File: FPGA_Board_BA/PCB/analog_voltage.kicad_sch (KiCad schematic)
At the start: 10 parts, among them U8 TPS61022

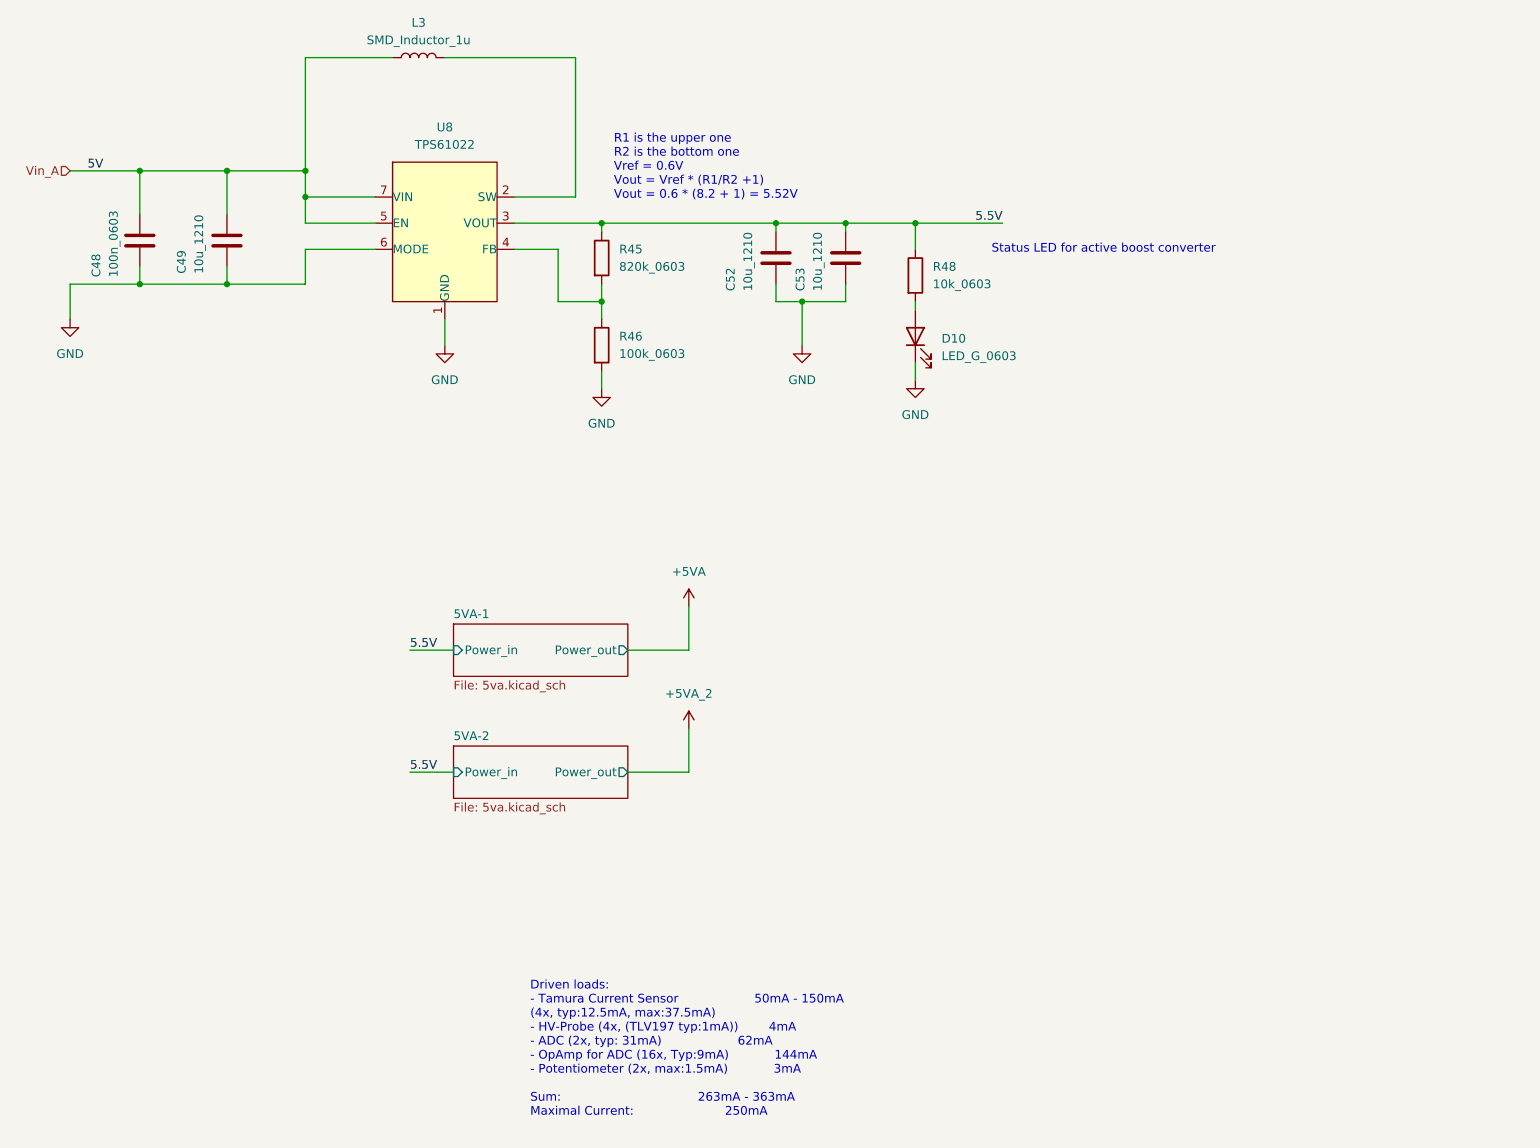
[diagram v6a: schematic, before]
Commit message: added 5V supply for Zynq
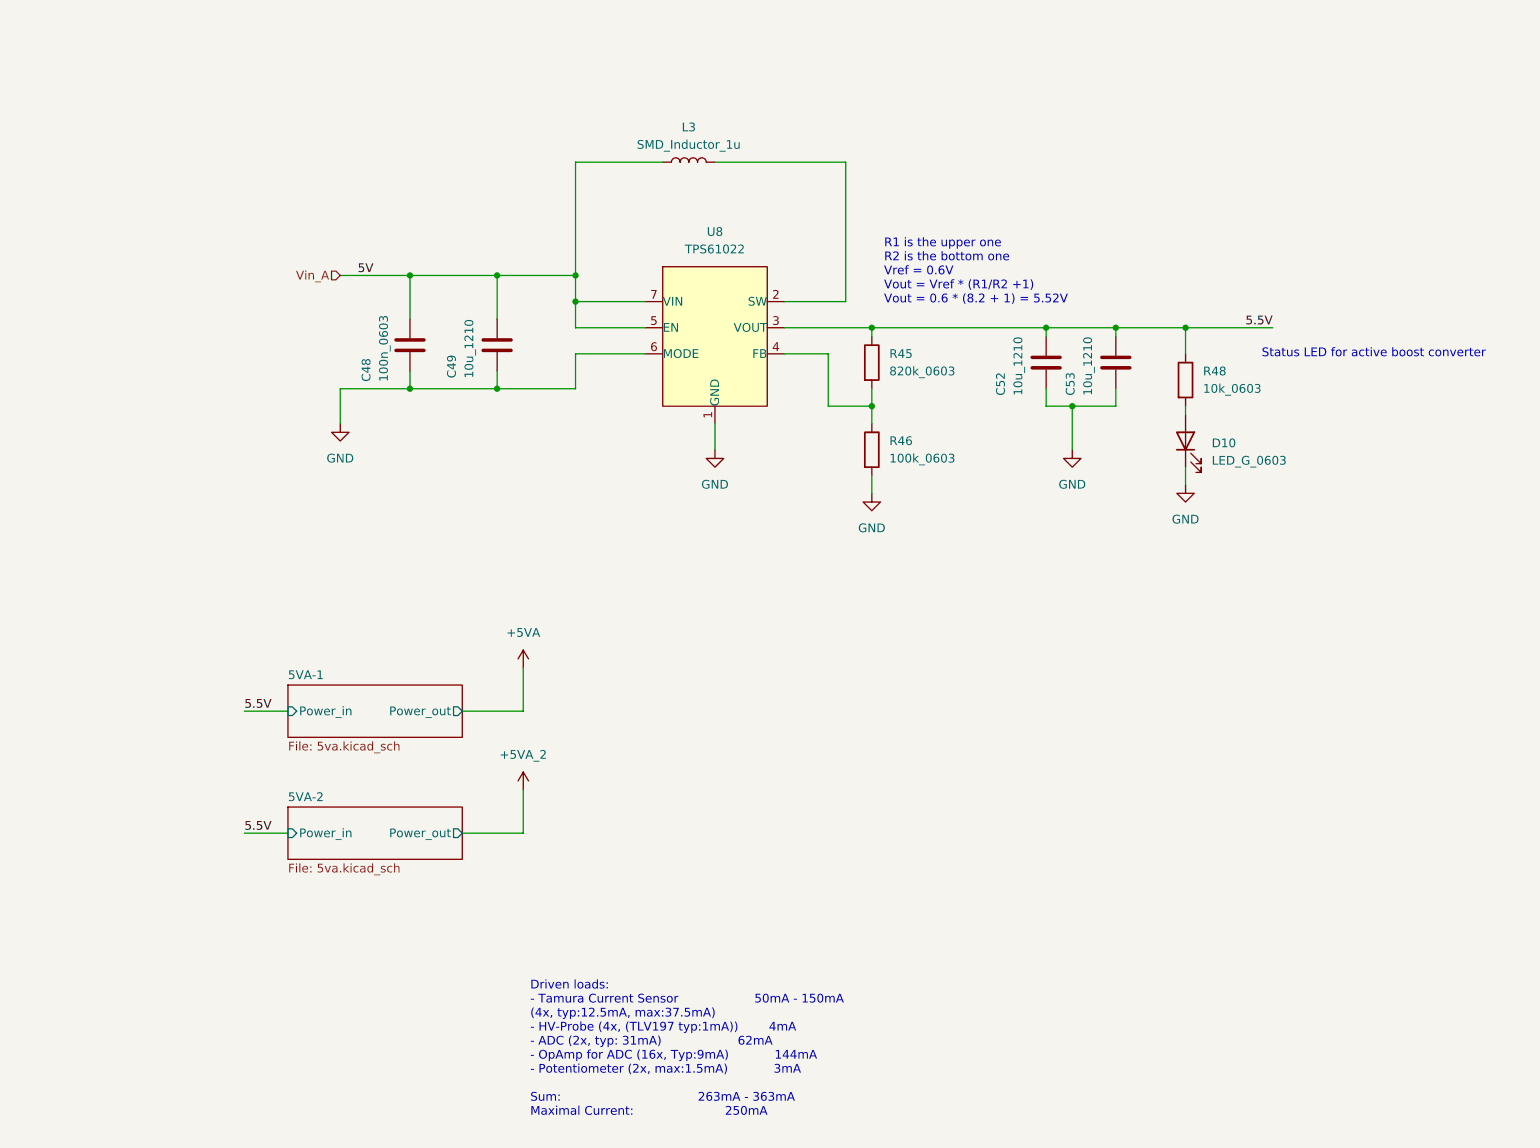
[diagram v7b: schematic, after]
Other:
- moved on the sheet: C48, C49, C52, C53, D10, L3, R45, R46, R48, U8
